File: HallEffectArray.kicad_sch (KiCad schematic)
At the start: 46 parts

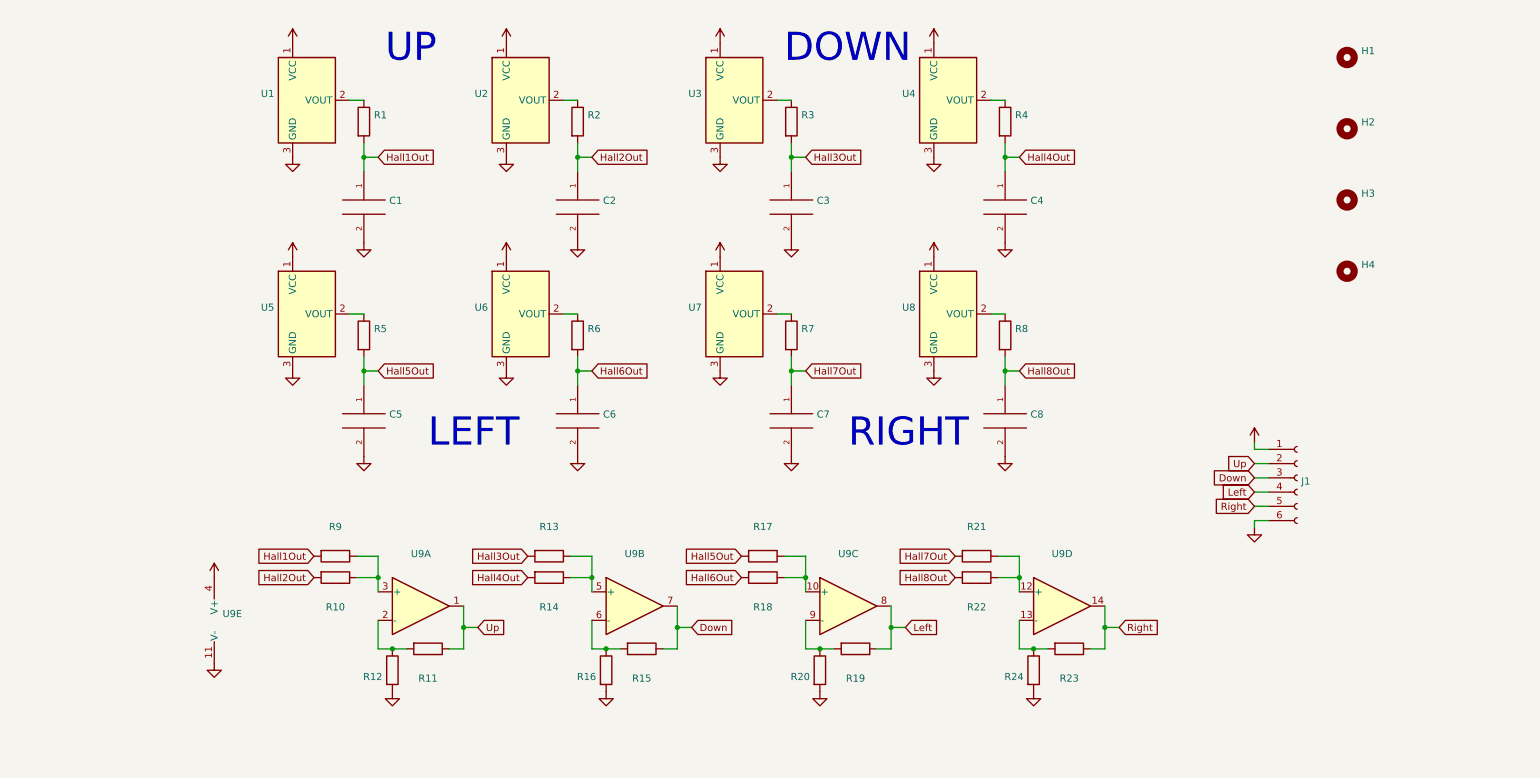
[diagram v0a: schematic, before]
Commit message: Version 1.2: Added trimmer pots, bypass capacitors, vias, board size now 100x100mm
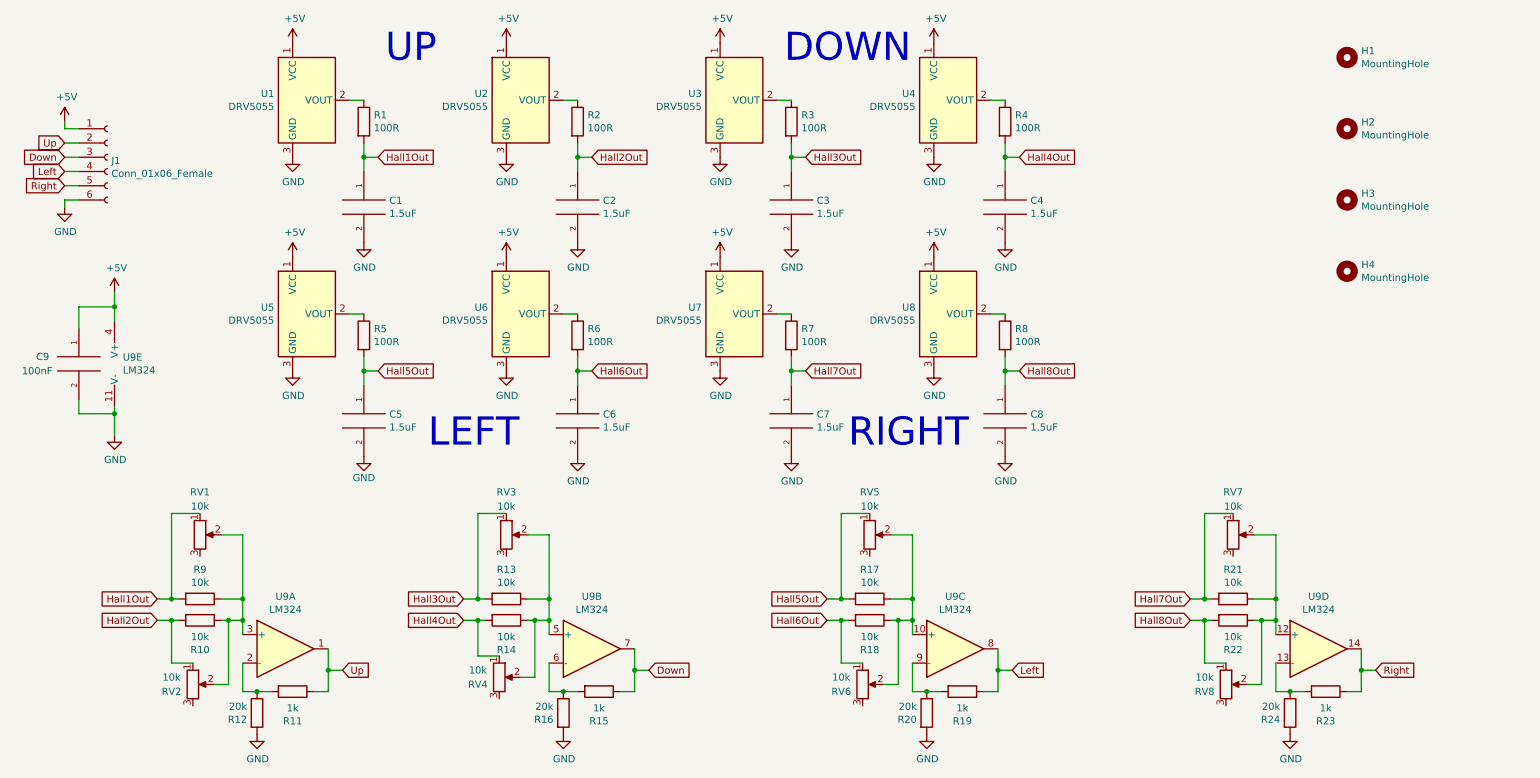
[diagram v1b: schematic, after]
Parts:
- added C9: 100nF, Capacitor_SMD:C_0805_2012Metric, symbol pspice:C
- added RV1, RV2, RV3, RV4, RV5, RV6, RV7, RV8: 10k, Potentiometer_SMD:Potentiometer_Bourns_TC33X_Vertical, symbol Device:R_Potentiometer
- C1, C2, C3, C4, C5, C6, C7, C8: value (none) -> 1.5uF; footprint (none) -> Capacitor_SMD:C_0805_2012Metric
- H1, H2, H3, H4: value (none) -> MountingHole; footprint (none) -> MountingHole:MountingHole_2.7mm_M2.5
- J1: value (none) -> Conn_01x06_Female; footprint (none) -> Connector_JST:JST_XH_B6B-XH-A_1x06_P2.50mm_Vertical
- R1, R2, R3, R4, R5, R6, R7, R8: value (none) -> 100R; footprint (none) -> Resistor_SMD:R_0805_2012Metric
- R10, R13, R14, R17, R18, R21, R22, R9: value (none) -> 10k; footprint (none) -> Resistor_SMD:R_0805_2012Metric
- R11, R15, R19, R23: value (none) -> 1k; footprint (none) -> Resistor_SMD:R_0805_2012Metric
- R12, R16, R20, R24: value (none) -> 20k; footprint (none) -> Resistor_SMD:R_0805_2012Metric
- U1, U2, U3, U4, U5, U6, U7, U8: value (none) -> DRV5055; footprint (none) -> Package_TO_SOT_SMD:SOT-23
- U9: value (none) -> LM324; footprint (none) -> Package_SO:SOIC-14_3.9x8.7mm_P1.27mm
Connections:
- net +5V: now also C9.1
- net GND: now also C9.2
- net Hall1Out: now also RV1.1
- net Hall2Out: now also RV2.1
- net Hall3Out: now also RV3.1
- net Hall4Out: now also RV4.1
- net Hall5Out: now also RV5.1
- net Hall6Out: now also RV6.1
- net Hall7Out: now also RV7.1
- net Hall8Out: now also RV8.1
- net at R10.1, R9.1, U9.3 (+): now also RV1.2, RV2.2
- net at R13.1, R14.1, U9.5 (+): now also RV3.2, RV4.2
- net at R17.1, R18.1, U9.10 (+): now also RV5.2, RV6.2
- net at R21.1, R22.1, U9.12 (+): now also RV7.2, RV8.2
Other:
- moved on the sheet: J1, R10, R11, R12, R13, R14, R15, R16, R17, R18, R19, R20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

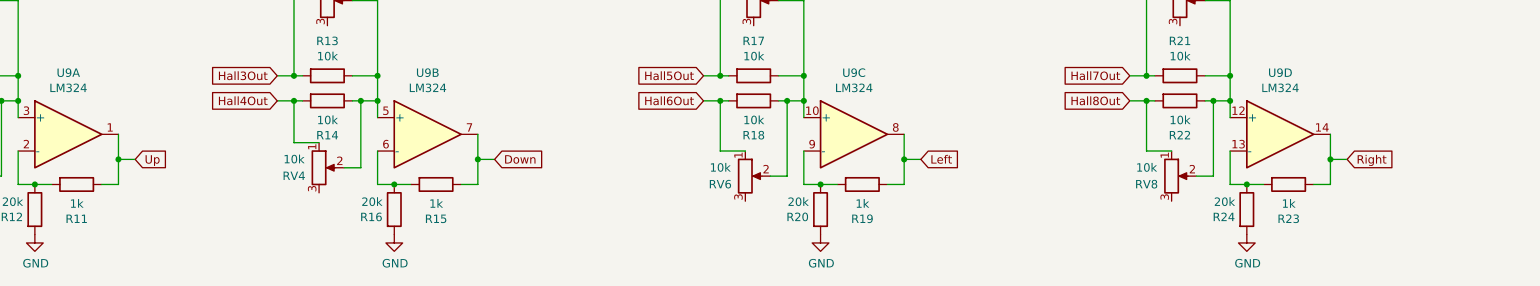
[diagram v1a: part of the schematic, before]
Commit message: V1.3: Added decoupling caps on outputs, more vias, changed datasheet
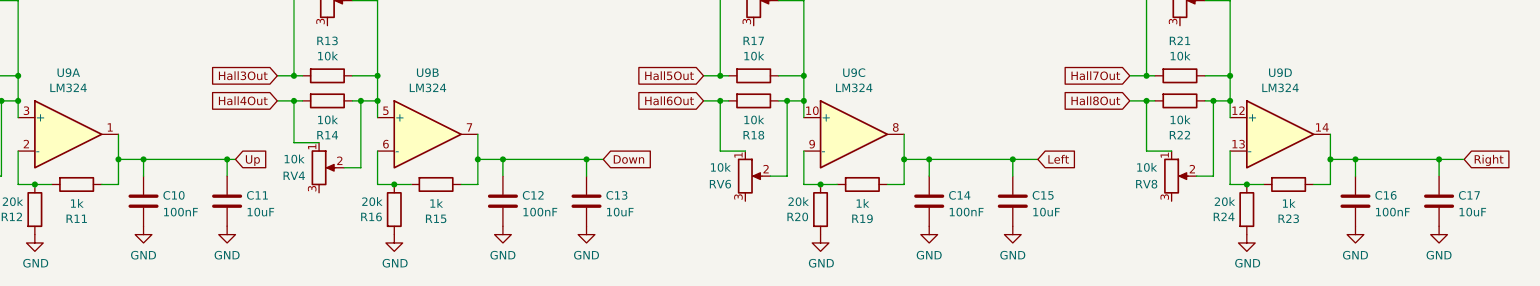
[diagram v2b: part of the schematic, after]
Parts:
- added C10, C12, C14, C16: 100nF, Capacitor_SMD:C_0805_2012Metric, symbol Device:C
- added C11, C13, C15, C17: 10uF, Capacitor_SMD:C_0805_2012Metric, symbol Device:C
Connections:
- net Down: now also C12.1, C13.1
- net GND: now also C10.2, C11.2, C12.2, C13.2, C14.2, C15.2, C16.2, C17.2
- net Left: now also C14.1, C15.1
- net Right: now also C16.1, C17.1
- net Up: now also C10.1, C11.1
